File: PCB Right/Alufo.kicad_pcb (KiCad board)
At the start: 2 copper layers, 282.6 x 90.9 mm, 93 parts, among them J2 USB_C_Receptacle_USB2.0_16P_2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, J4 USB_C_Receptacle_USB2.0_16P_2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, K11 PG1350, K12 PG1350, K13 PG1350, K14 PG1350, K15 PG1350, K16 PG1350, K21 PG1350, K22 PG1350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

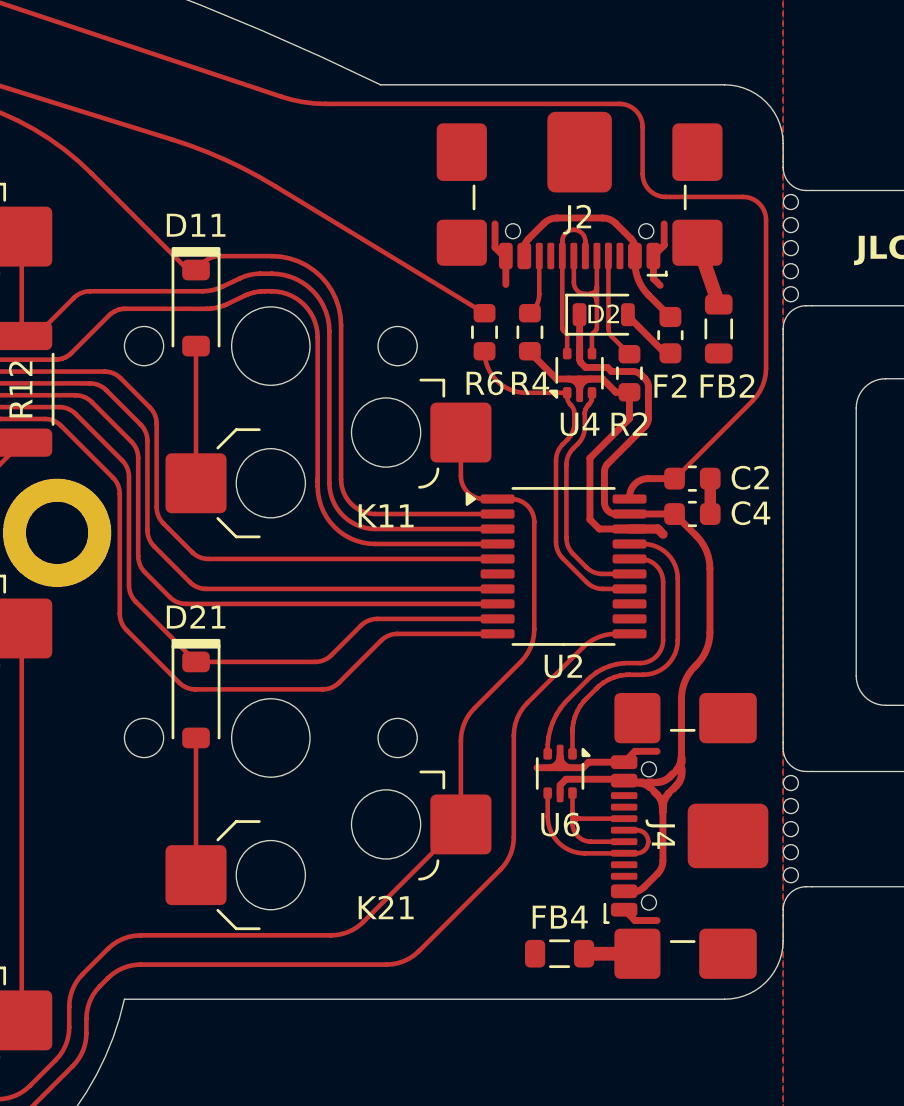
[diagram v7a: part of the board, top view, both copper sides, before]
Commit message: Add shield connectors
The USB ports will now be connected to the aluminium PCB core. This is done using a 0.6mm diameter wire. One end of the wire will be soldered to a pad on the PCB and the other will pass through a hole to friction fit against the aluminium core.

Also, R9, the 0Ω resistor on the lefthand VCC line has returned to allow a more direct ground route between the USB port and the MCU. However it is now a smaller 0805 size resistor.
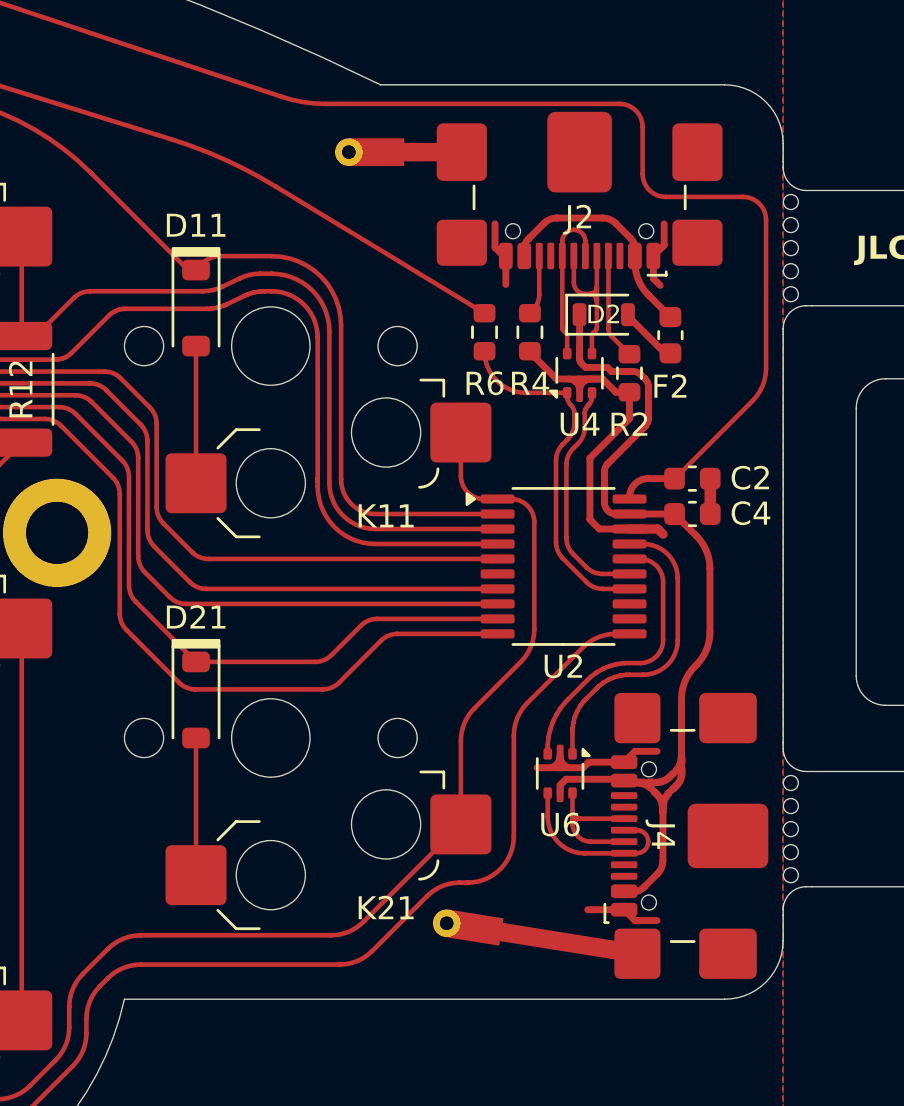
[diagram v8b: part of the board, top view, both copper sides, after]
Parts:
- removed FB2, FB4: FerriteBead, Inductor_SMD:L_0805_2012Metric
- added J6: Shield_Connection, Project_Library:Shield_Connector, F.Cu at (147.2, 44.0)
- added J8: Shield_Connection, Project_Library:Shield_Connector, F.Cu at (151.4, 77.6)
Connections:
- J2 pad S2: Net-(FB2-Pad1) -> unconnected-(J2-SHIELD-PadS2)
- J2 pad S4: unconnected-(J2-SHIELD-PadS4) -> Net-(J6-Pin_1)
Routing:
- net Net-(J8-Pin_1): track 2.31 -> 7.18 mm
- net Net-(J6-Pin_1): track 0.00 -> 3.70 mm
- net Net-(FB2-Pad1): track 2.83 -> 0.00 mm
- net GND: track 25.9 -> 27.5 mm
